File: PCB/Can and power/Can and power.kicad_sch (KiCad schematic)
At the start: 38 parts, among them J1 TPS54232DR, J2 ESP32, J3 12V, J4 C_H, J5 C_L, J6 GND, U1 SN65HVD230

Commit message: Schematics and PCB update
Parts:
- D1, D2: footprint SamacSys_Parts:DIONC1005X43N -> DIY:DIONC1005X43N; symbol SamacSys_Parts:PESD0402-140 -> DIY:PESD0402-140
- D3: footprint SamacSys_Parts:SODFL3617X108N -> DIY:SODFL3617X108N; symbol SamacSys_Parts:SS24FL -> DIY:SS24FL
- J1: footprint SamacSys_Parts:SOIC127P600X175-8N -> DIY:SOIC127P600X175-8N; symbol SamacSys_Parts:TPS54232DR -> DIY:TPS54232DR
- L2: footprint SamacSys_Parts:INDC6060X450N -> DIY:INDC6060X450N; symbol SamacSys_Parts:SRN6045TA-150M -> DIY:SRN6045TA-150M
- renumbered C6 to C1, C6 to C2

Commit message: CanPower v5.1 preparation
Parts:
- added JP4: Use IGN, Jumper:SolderJumper-2_P1.3mm_Bridged_RoundedPad1.0x1.5mm, symbol Jumper:SolderJumper_2_Bridged
- JP1, JP2, JP3: now left out of the parts list
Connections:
- net at Ren1.1, Ren2.2: now also JP4.1 (A); no longer J1.3 (EN)
- new net: J1.3 (EN), JP4.2 (B)
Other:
- moved on the sheet: J2, Ren1, Ren2

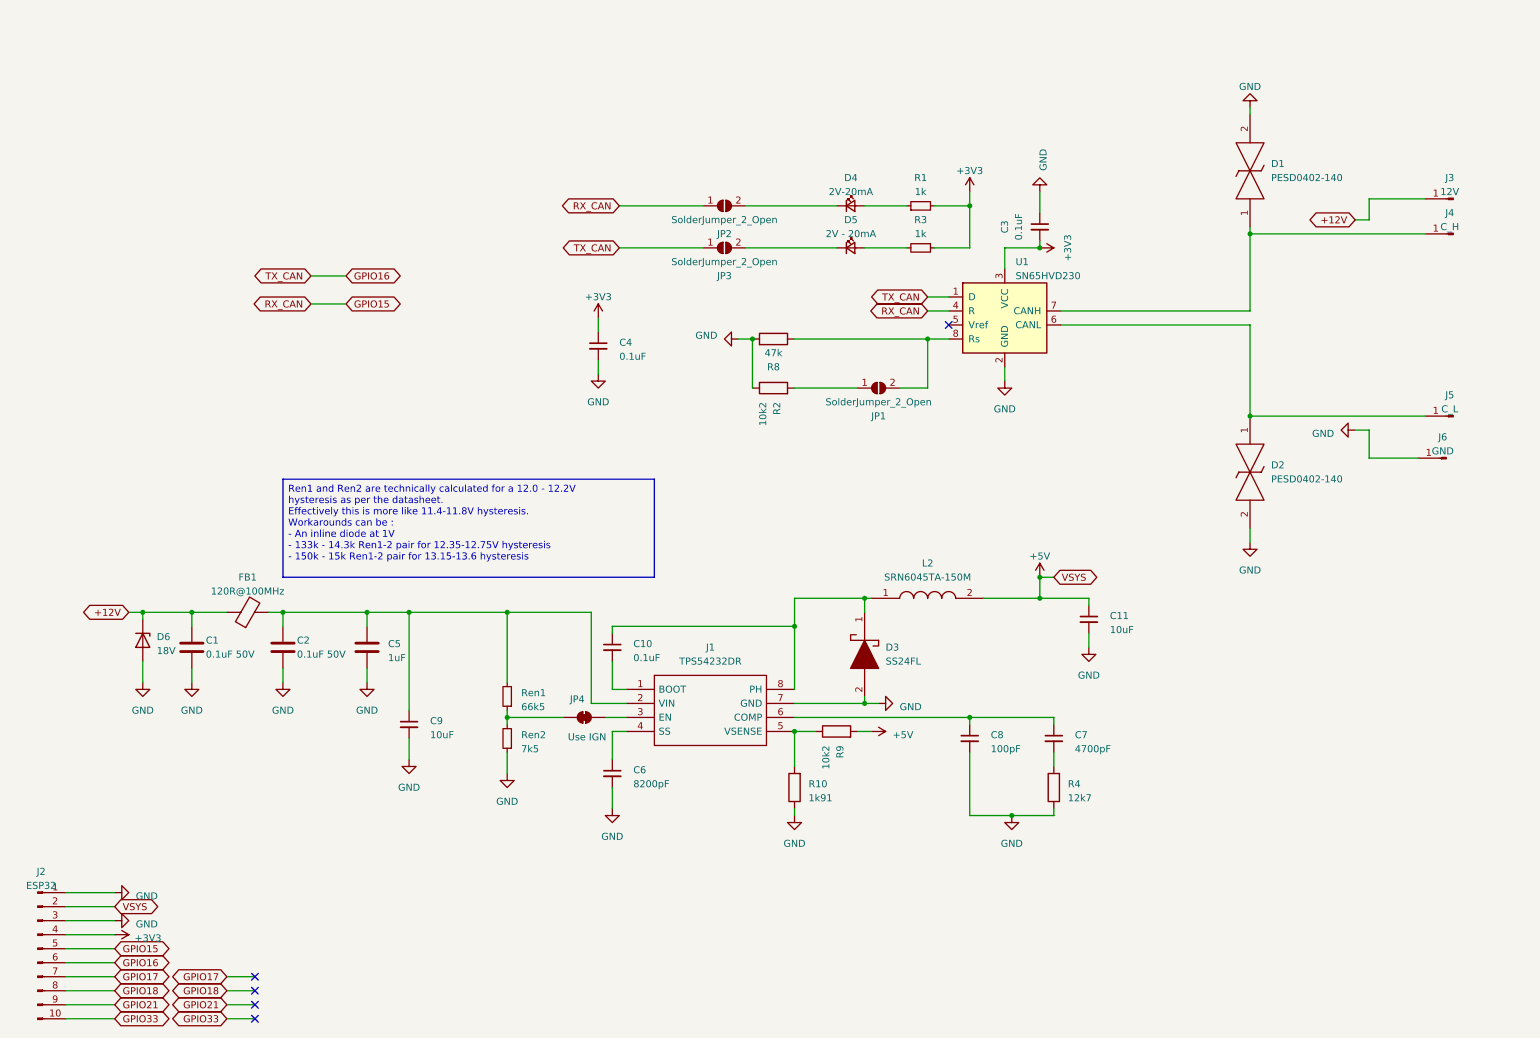
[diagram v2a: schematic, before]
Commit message: Partial schematic update
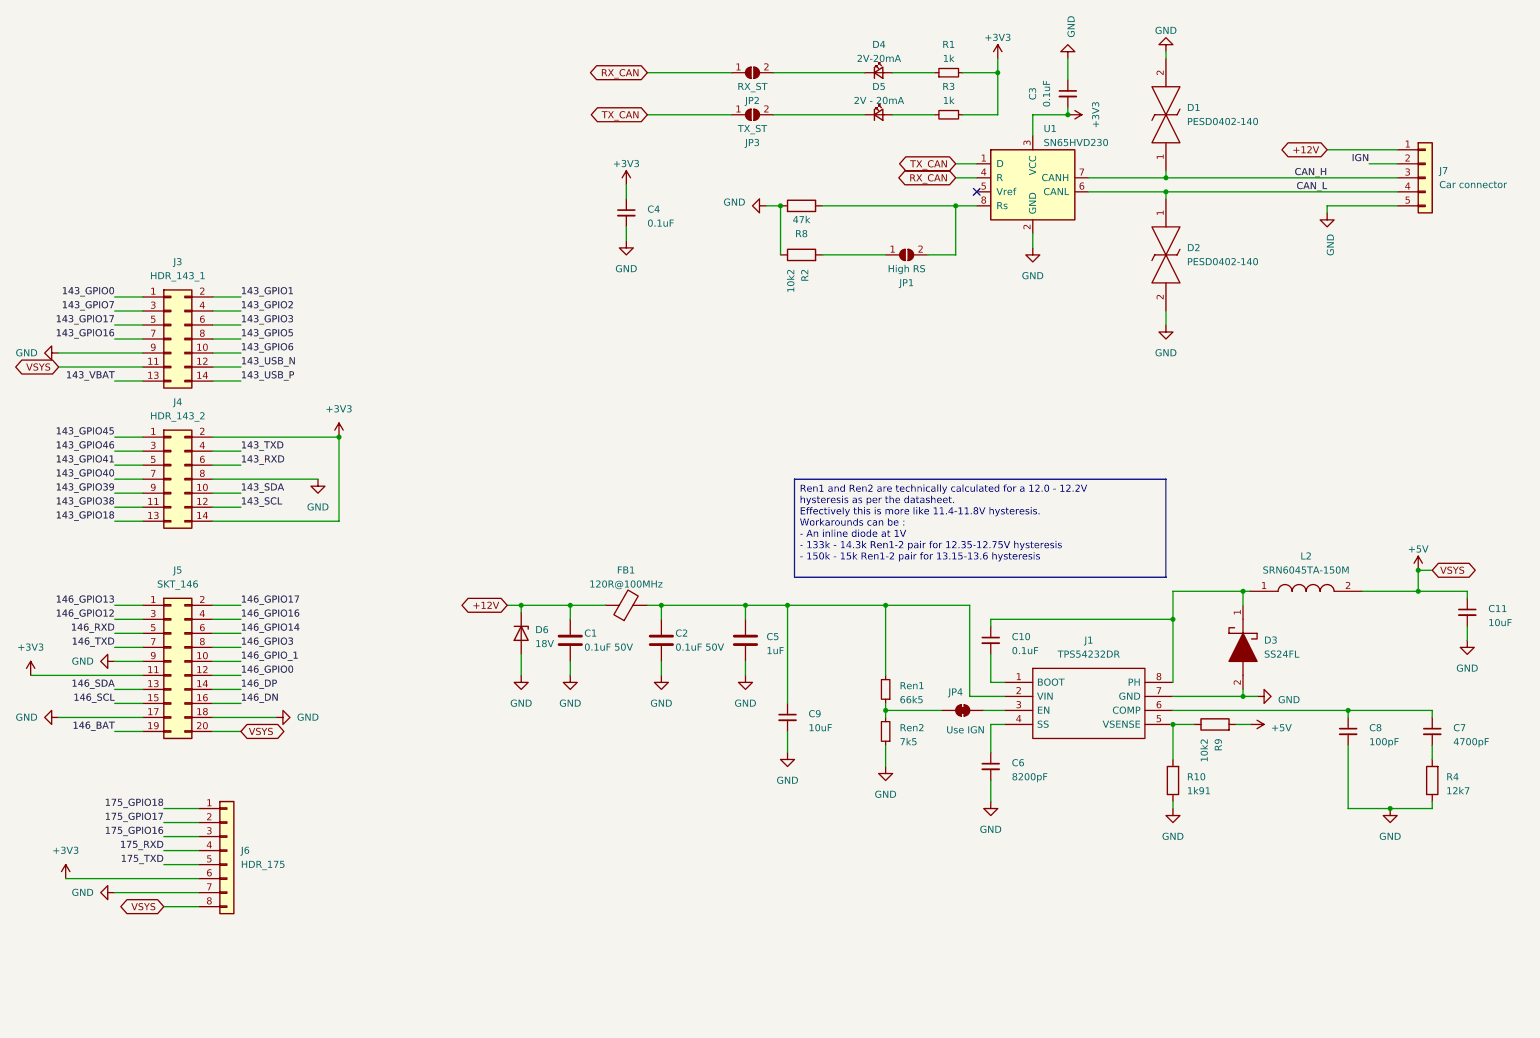
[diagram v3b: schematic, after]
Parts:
- removed J2: ESP32, Connector_PinHeader_2.54mm:PinHeader_1x10_P2.54mm_Vertical, symbol Connector:Conn_01x10_Pin
- removed J3: 12V, Connector_PinHeader_2.54mm:PinHeader_1x01_P2.54mm_Vertical, symbol Connector:Conn_01x01_Pin
- removed J4: C_H, Connector_PinHeader_2.54mm:PinHeader_1x01_P2.54mm_Vertical, symbol Connector:Conn_01x01_Pin
- removed J5: C_L, Connector_PinHeader_2.54mm:PinHeader_1x01_P2.54mm_Vertical, symbol Connector:Conn_01x01_Pin
- removed J6: GND, Connector_PinHeader_2.54mm:PinHeader_1x01_P2.54mm_Vertical, symbol Connector:Conn_01x01_Pin
- added J3: HDR_143_1, Connector_PinSocket_1.27mm:PinSocket_2x07_P1.27mm_Vertical, symbol Connector_Generic:Conn_02x07_Odd_Even
- added J4: HDR_143_2, Connector_PinSocket_1.27mm:PinSocket_2x07_P1.27mm_Vertical, symbol Connector_Generic:Conn_02x07_Odd_Even
- added J5: SKT_146, Connector_PinSocket_1.27mm:PinSocket_2x10_P1.27mm_Vertical, symbol Connector_Generic:Conn_02x10_Odd_Even
- added J6: HDR_175, Connector_PinSocket_2.54mm:PinSocket_1x08_P2.54mm_Vertical, symbol Connector_Generic:Conn_01x08
- added J7: Car connector, Connector_PinHeader_2.54mm:PinHeader_1x05_P2.54mm_Vertical, symbol Connector_Generic:Conn_01x05
- JP1: value SolderJumper_2_Open -> High RS
- JP2: value SolderJumper_2_Open -> RX_ST
- JP3: value SolderJumper_2_Open -> TX_ST
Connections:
- net +12V: now also J7.1 (Pin_1)
- net +3V3: now also J4.14 (Pin_14), J4.2 (Pin_2), J5.11 (Pin_11), J6.6 (Pin_6)
- net +5V: now also J3.11 (Pin_11), J5.20 (Pin_20), J6.8 (Pin_8)
- net GND: now also J3.9 (Pin_9), J4.8 (Pin_8), J5.17 (Pin_17), J5.18 (Pin_18), J5.9 (Pin_9), J6.7 (Pin_7), J7.5 (Pin_5)
- net CAN_L: now reaches D2.1, U1.6 (CANL)
- net CAN_L: now also J7.4 (Pin_4)
- net CAN_H: now reaches D1.1, U1.7 (CANH)
- net CAN_H: now also J7.3 (Pin_3)
- net GPIO15 renamed RX_CAN
- net GPIO16 renamed TX_CAN
- new net 143_GPIO0: J3.1 (Pin_1)
- new net 143_GPIO1: J3.2 (Pin_2)
- new net 143_GPIO16: J3.7 (Pin_7)
- new net 143_GPIO17: J3.5 (Pin_5)
- new net 143_GPIO18: J4.13 (Pin_13)
- new net 143_GPIO2: J3.4 (Pin_4)
- new net 143_GPIO3: J3.6 (Pin_6)
- new net 143_GPIO38: J4.11 (Pin_11)
- new net 143_GPIO39: J4.9 (Pin_9)
- new net 143_GPIO40: J4.7 (Pin_7)
- new net 143_GPIO41: J4.5 (Pin_5)
- new net 143_GPIO45: J4.1 (Pin_1)
- new net 143_GPIO46: J4.3 (Pin_3)
- new net 143_GPIO5: J3.8 (Pin_8)
- new net 143_GPIO6: J3.10 (Pin_10)
- new net 143_GPIO7: J3.3 (Pin_3)
- new net 143_RXD: J4.6 (Pin_6)
- new net 143_SCL: J4.12 (Pin_12)
- new net 143_SDA: J4.10 (Pin_10)
- new net 143_TXD: J4.4 (Pin_4)
- new net 143_USB_N: J3.12 (Pin_12)
- new net 143_USB_P: J3.14 (Pin_14)
- new net 143_VBAT: J3.13 (Pin_13)
- new net 146_BAT: J5.19 (Pin_19)
- new net 146_DN: J5.16 (Pin_16)
- new net 146_DP: J5.14 (Pin_14)
- new net 146_GPIO0: J5.12 (Pin_12)
- new net 146_GPIO12: J5.3 (Pin_3)
- new net 146_GPIO13: J5.1 (Pin_1)
- new net 146_GPIO14: J5.6 (Pin_6)
- new net 146_GPIO16: J5.4 (Pin_4)
- new net 146_GPIO17: J5.2 (Pin_2)
- new net 146_GPIO3: J5.8 (Pin_8)
- new net 146_GPIO_1: J5.10 (Pin_10)
- new net 146_RXD: J5.5 (Pin_5)
- new net 146_SCL: J5.15 (Pin_15)
- new net 146_SDA: J5.13 (Pin_13)
- new net 146_TXD: J5.7 (Pin_7)
- new net 175_GPIO16: J6.3 (Pin_3)
- new net 175_GPIO17: J6.2 (Pin_2)
- new net 175_GPIO18: J6.1 (Pin_1)
- new net 175_RXD: J6.4 (Pin_4)
- new net 175_TXD: J6.5 (Pin_5)
- new net IGN: J7.2 (Pin_2)
- no-connect marks 5 -> 1
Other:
- moved on the sheet: C1, C10, C11, C2, C3, C4, C5, C6, C7, C8, C9, D1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

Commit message: Pre-PCB layout
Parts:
- removed JP2: RX_ST, Jumper:SolderJumper-2_P1.3mm_Open_RoundedPad1.0x1.5mm, symbol Jumper:SolderJumper_2_Open
- removed JP3: TX_ST, Jumper:SolderJumper-2_P1.3mm_Open_RoundedPad1.0x1.5mm, symbol Jumper:SolderJumper_2_Open
- J7: footprint Connector_PinHeader_2.54mm:PinHeader_1x05_P2.54mm_Vertical -> Connector_PinHeader_2.54mm:PinHeader_1x04_P2.54mm_Vertical; symbol Connector_Generic:Conn_01x05 -> Connector_Generic:Conn_01x04
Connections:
- net IGN is gone; now on net CAN_H: J7.2 (Pin_2)
- net CAN_H: no longer J7.3 (Pin_3)
- net CAN_L: now also J7.3 (Pin_3); no longer J7.4 (Pin_4)
- net GND: now also J7.4 (Pin_4); no longer J7.5 (Pin_5)
- net RX_CAN: now also D4.1 (K)
- net TX_CAN: now also D5.1 (K)
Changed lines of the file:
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@@
 	(wire
 		(pts
-			(xy 127 31.75) (xy 142.24 31.75)
-		)
-		(stroke
-			(width 0)
-			(type default)
-		)
-	)
-	(wire
-		(pts
-			(xy 149.86 24.13) (xy 166.37 24.13)
+			(xy 127 31.75) (xy 166.37 31.75)
 		)
 		(stroke
@@
 	(wire
 		(pts
-			(xy 149.86 31.75) (xy 166.37 31.75)
-		)
-		(stroke
-			(width 0)
-			(type default)
-		)
-	)
-	(wire
-		(pts
 			(xy 190.5 24.13) (xy 190.5 21.59)
 		)
@@
 	(wire
 		(pts
-			(xy 127 24.13) (xy 142.24 24.13)
+			(xy 127 24.13) (xy 166.37 24.13)
 		)
 		(stroke
@@
 	(wire
 		(pts
-			(xy 207.01 45.72) (xy 220.98 45.72)
+			(xy 250.19 40.64) (xy 262.89 40.64)
 		)
 		(stroke
@@
 	(wire
 		(pts
-			(xy 257.81 40.64) (xy 262.89 40.64)
+			(xy 207.01 45.72) (xy 220.98 45.72)
 		)
 		(stroke
@@
 	(wire
 		(pts
+			(xy 250.19 36.83) (xy 250.19 40.64)
+		)
+		(stroke
+			(width 0)
+			(type default)
+		)
+	)
+	(wire
+		(pts
 			(xy 191.77 134.62) (xy 189.23 134.62)
 		)
@@
 	(wire
 		(pts
-			(xy 250.19 38.1) (xy 262.89 38.1)
-		)
-		(stroke
-			(width 0)
-			(type default)
-		)
-	)
-	(wire
-		(pts
 			(xy 48.26 102.87) (xy 53.34 102.87)
 		)
@@
 		)
 	)
-	(label "IGN"
-		(at 257.81 40.64 180)
-		(effects
-			(font
-				(size 1.27 1.27)
-			)
-			(justify right bottom)
-		)
-	)
 	(label "CAN_L"
 		(at 250.19 45.72 180)
@@
 	(global_label "+12V"
 		(shape bidirectional)
-		(at 250.19 38.1 180)
+		(at 250.19 36.83 90)
 		(fields_autoplaced yes)
 		(effects
@@
 				(size 1.27 1.27)
 			)
-			(justify right)
+			(justify left)
 		)
 		(property "Intersheetrefs" "${INTERSHEET_REFS}"
-			(at 241.9059 38.1 0)
+			(at 250.19 28.4665 90)
 			(effects
 				(font
 					(size 1.27 1.27)
 				)
-				(justify right)
+				(justify left)
 				(hide yes)
 			)
@@
 	)
 	(symbol
-		(lib_id "Jumper:SolderJumper_2_Open")
-		(at 146.05 31.75 0)
-		(mirror x)
-		(unit 1)
-		(exclude_from_sim no)
-		(in_bom no)
-		(on_board yes)
-		(dnp no)
-		(property "Reference" "JP3"
-			(at 146.05 36.83 0)
-			(effects
-				(font
-					(size 1.27 1.27)
-				)
-			)
-		)
-		(property "Value" "TX_ST"
-			(at 146.05 34.29 0)
-			(effects
-				(font
-					(size 1.27 1.27)
-				)
-			)
-		)
-		(property "Footprint" "Jumper:SolderJumper-2_P1.3mm_Open_RoundedPad1.0x1.5mm"
-			(at 146.05 31.75 0)
-			(effects
-				(font
-					(size 1.27 1.27)
-				)
-				(hide yes)
-			)
-		)
-		(property "Datasheet" "~"
-			(at 146.05 31.75 0)
-			(effects
-				(font
-					(size 1.27 1.27)
-				)
-				(hide yes)
-			)
-		)
-		(property "Description" ""
-			(at 146.05 31.75 0)
-			(effects
-				(font
-					(size 1.27 1.27)
-				)
-			)
-		)
-		(property "MPN" ""
-			(at 146.05 31.75 0)
-			(effects
-				(font
-					(size 1.27 1.27)
-				)
-				(hide yes)
-			)
-		)
-		(property "Package" ""
-			(at 146.05 31.75 0)
-			(effects
-				(font
-					(size 1.27 1.27)
-				)
-				(hide yes)
-			)
-		)
-		(pin "1"
-		)
-		(pin "2"
-		)
-		(instances
-			(project "Can and power"
-				(path "/81a7cfcd-072f-485b-9296-819a4dd752de"
-					(reference "JP3")
-					(unit 1)
-				)
-			)
-		)
-	)
-	(symbol
 		(lib_id "Jumper:SolderJumper_2_Bridged")
 		(at 184.15 139.7 0)
@@
 	)
 	(symbol
-		(lib_id "Connector_Generic:Conn_01x05")
+		(lib_id "Connector_Generic:Conn_01x04")
 		(at 267.97 43.18 0)
 		(unit 1)
@@
 		(fields_autoplaced yes)
 		(property "Reference" "J7"
-			(at 270.51 41.9099 0)
+			(at 270.51 43.1799 0)
 			(effects
 				(font
@@
 		)
 		(property "Value" "Car connector"
-			(at 270.51 44.4499 0)
+			(at 270.51 45.7199 0)
 			(effects
 				(font
@@
 			)
 		)
-		(property "Footprint" "Connector_PinHeader_2.54mm:PinHeader_1x05_P2.54mm_Vertical"
+		(property "Footprint" "Connector_PinHeader_2.54mm:PinHeader_1x04_P2.54mm_Vertical"
 			(at 267.97 43.18 0)
 			(effects
@@
 			)
 		)
-		(property "Description" "Generic connector, single row, 01x05, script generated (kicad-library-utils/schlib/autogen/connector/)"
+		(property "Description" "Generic connector, single row, 01x04, script generated (kicad-library-utils/schlib/autogen/connector/)"
 			(at 267.97 43.18 0)
 			(effects
@@
 		(pin "1"
 		)
-		(pin "5"
-		)
 		(pin "2"
 		)
@@
 					(unit 1)
 				)
-			)
-		)
-	)
-	(symbol
-		(lib_id "Jumper:SolderJumper_2_Open")
-		(at 146.05 24.13 0)
-		(mirror x)
-		(unit 1)
-		(exclude_from_sim no)
-		(in_bom no)
-		(on_board yes)
-		(dnp no)
-		(property "Reference" "JP2"
-			(at 146.05 29.21 0)
-			(effects
-				(font
-					(size 1.27 1.27)
-				)
-			)
-		)
-		(property "Value" "RX_ST"
-			(at 146.05 26.67 0)
-			(effects
-				(font
-					(size 1.27 1.27)
-				)
-			)
-		)
-		(property "Footprint" "Jumper:SolderJumper-2_P1.3mm_Open_RoundedPad1.0x1.5mm"
-			(at 146.05 24.13 0)
-			(effects
-				(font
-					(size 1.27 1.27)
-				)
-				(hide yes)
-			)
-		)
-		(property "Datasheet" "~"
-			(at 146.05 24.13 0)
-			(effects
-				(font
-					(size 1.27 1.27)
-				)
-				(hide yes)
-			)
-		)
-		(property "Description" ""
-			(at 146.05 24.13 0)
-			(effects
-				(font
-					(size 1.27 1.27)
-				)
-			)
-		)
-		(property "MPN" ""
-			(at 146.05 24.13 0)
-			(effects
-				(font
-					(size 1.27 1.27)
-				)
-				(hide yes)
-			)
-		)
-		(property "Package" ""
-			(at 146.05 24.13 0)
-			(effects
-				(font
-					(size 1.27 1.27)
-				)
-				(hide yes)
-			)
-		)
-		(pin "1"
-		)
-		(pin "2"
-		)
-		(instances
-			(project "Can and power"
-				(path "/81a7cfcd-072f-485b-9296-819a4dd752de"
-					(reference "JP2")
-					(unit 1)
-				)

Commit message: Need ERC corrections
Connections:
- net 143_GPIO2 is gone; now on net RX_CAN: J3.4 (Pin_4)
- net 143_GPIO3 is gone; now on net TX_CAN: J3.6 (Pin_6)
- net 146_GPIO12 is gone; now on net RX_CAN: J5.3 (Pin_3)
- net 146_GPIO13 is gone; now on net TX_CAN: J5.1 (Pin_1)
- net 175_RXD is gone; now on net RX_CAN: J6.4 (Pin_4)
- net 175_TXD is gone; now on net TX_CAN: J6.5 (Pin_5)
- no-connect marks 1 -> 38

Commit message: Projectification, correct footprints
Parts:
- added F1: 30V 500mA 2.5A-100ms, Fuse:Fuse_1210_3225Metric, symbol Device:Polyfuse_Small
- added RV1: B72520T0140K062, Fuse:Fuse_1206_3216Metric, symbol Device:Varistor
- D1, D2: footprint DIY:DIONC1005X43N -> Project_footprints:DIONC1005X43N; symbol DIY:PESD0402-140 -> Symbols:PESD0402-140
- D3: footprint DIY:SODFL3617X108N -> Project_footprints:SODFL3617X108N; symbol DIY:SS24FL -> Symbols:SS24FL
- J1: footprint DIY:SOIC127P600X175-8N -> Project_footprints:SOIC127P600X175-8N; symbol DIY:TPS54232DR -> Symbols:TPS54232DR
- J3, J4: footprint Connector_PinSocket_1.27mm:PinSocket_2x07_P1.27mm_Vertical -> Connector_PinHeader_1.27mm:PinHeader_2x07_P1.27mm_Vertical
- J6: footprint Connector_PinSocket_2.54mm:PinSocket_1x08_P2.54mm_Vertical -> Connector_PinHeader_2.54mm:PinHeader_1x08_P2.54mm_Vertical
- J7: footprint Connector_PinHeader_2.54mm:PinHeader_1x04_P2.54mm_Vertical -> Connector_JST:JST_EH_B4B-EH-A_1x04_P2.50mm_Vertical
- L2: footprint DIY:INDC6060X450N -> Project_footprints:INDC6060X450N; symbol DIY:SRN6045TA-150M -> Symbols:SRN6045TA-150M
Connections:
- net +12V: now also F1.1; no longer C1.2, D6.1 (K), FB1.1
- net +3V3: now also J4.1 (Pin_1), J4.13 (Pin_13); no longer J4.14 (Pin_14), J4.2 (Pin_2)
- net +5V: now also J3.12 (Pin_12); no longer J3.11 (Pin_11)
- net 143_GPIO0: now also J3.2 (Pin_2); no longer J3.1 (Pin_1)
- net 143_GPIO1: now also J3.1 (Pin_1); no longer J3.2 (Pin_2)
- net 143_GPIO16: now also J3.8 (Pin_8); no longer J3.7 (Pin_7)
- net 143_GPIO17: now also J3.6 (Pin_6); no longer J3.5 (Pin_5)
- net 143_GPIO18: now also J4.14 (Pin_14); no longer J4.13 (Pin_13)
- net 143_GPIO38: now also J4.12 (Pin_12); no longer J4.11 (Pin_11)
- net 143_GPIO39: now also J4.10 (Pin_10); no longer J4.9 (Pin_9)
- net 143_GPIO40: now also J4.8 (Pin_8); no longer J4.7 (Pin_7)
- net 143_GPIO41: now also J4.6 (Pin_6); no longer J4.5 (Pin_5)
- net 143_GPIO45: now also J4.2 (Pin_2); no longer J4.1 (Pin_1)
- net 143_GPIO46: now also J4.4 (Pin_4); no longer J4.3 (Pin_3)
- net 143_GPIO5: now also J3.7 (Pin_7); no longer J3.8 (Pin_8)
- net 143_GPIO6: now also J3.9 (Pin_9); no longer J3.10 (Pin_10)
- net 143_GPIO7: now also J3.4 (Pin_4); no longer J3.3 (Pin_3)
- net 143_RXD: now also J4.5 (Pin_5); no longer J4.6 (Pin_6)
- net 143_SCL: now also J4.11 (Pin_11); no longer J4.12 (Pin_12)
- net 143_SDA: now also J4.9 (Pin_9); no longer J4.10 (Pin_10)
- net 143_TXD: now also J4.3 (Pin_3); no longer J4.4 (Pin_4)
- net 143_USB_N: now also J3.11 (Pin_11); no longer J3.12 (Pin_12)
- net 143_USB_P: now also J3.13 (Pin_13); no longer J3.14 (Pin_14)
- net 143_VBAT: now also J3.14 (Pin_14); no longer J3.13 (Pin_13)
- net GND: now also J3.10 (Pin_10), J4.7 (Pin_7), RV1.2; no longer J3.9 (Pin_9), J4.8 (Pin_8)
- net RX_CAN: now also J3.3 (Pin_3); no longer J3.4 (Pin_4)
- net TX_CAN: now also J3.5 (Pin_5); no longer J3.6 (Pin_6)
- new net: C1.2, D6.1 (K), F1.2, FB1.1, RV1.1

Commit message: v6.1 placeholder for bulk resistor and capacitor
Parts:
- added C12: 0.1uF 50V, Capacitor_SMD:C_1206_3216Metric, symbol Device:C
- added R11: 100, Resistor_SMD:R_1206_3216Metric, symbol Device:R
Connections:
- net +12V: now also C12.2
- net GND: now also R11.1
- new net: C12.1, R11.2
